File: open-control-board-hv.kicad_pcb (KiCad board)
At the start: 2 copper layers, 69 x 54 mm, 20 parts, among them J1 TE 160650-2, J2 TE 160650-2, J3 TE 160650-2, J4 TE 160650-2, J5 TE 160650-2, J6 TE 160650-2, K1 RT314A12, U2 ALDP112, U3 ALDP112, U4 ALDP112

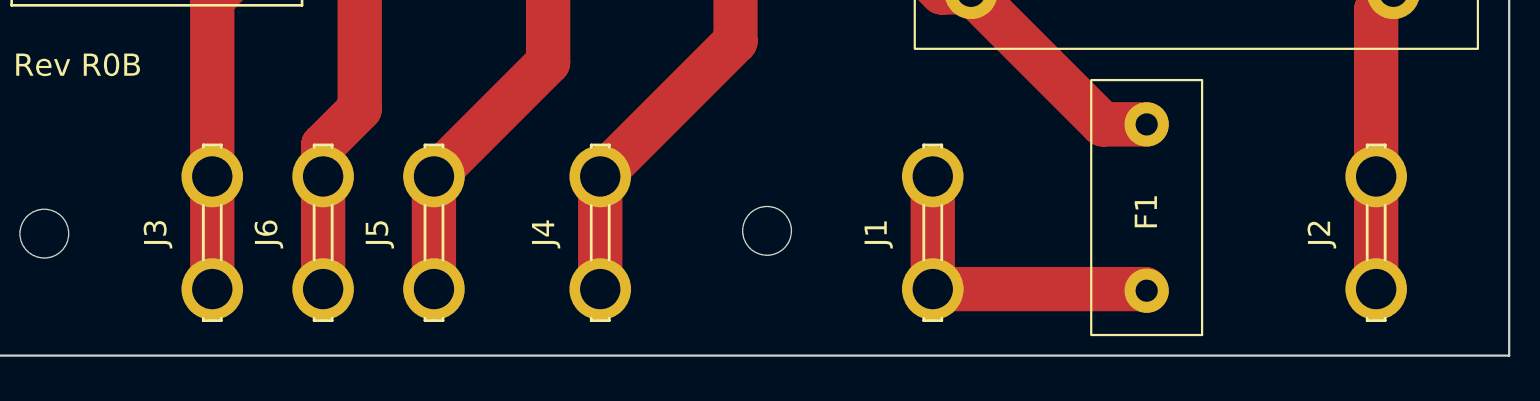
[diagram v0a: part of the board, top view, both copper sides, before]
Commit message: Updated with manufacturing data and switched footprint for fastons
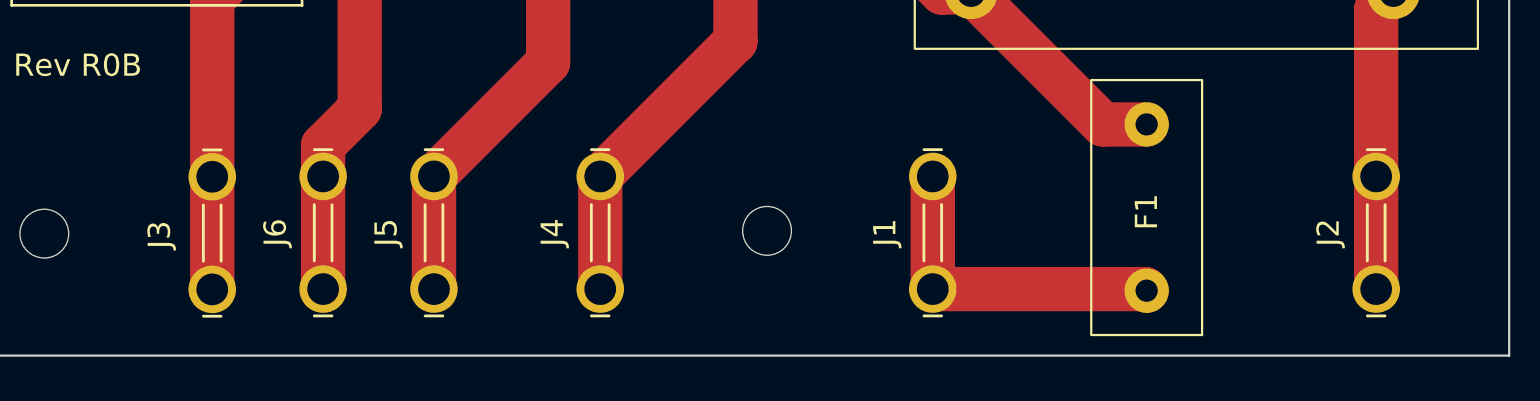
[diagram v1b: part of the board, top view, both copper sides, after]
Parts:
- J1, J2, J3, J4, J5, J6: footprint 1289:KEYSTONE_1289 -> 624091:TE_62409-1

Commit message: Cleanup
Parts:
- renumbered D4 to D2, D2 to D4, J6 to J4, J4 to J6, U4 to K2, U3 to K3, U2 to K4
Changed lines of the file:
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@@
     (property "ki_keywords" "connector")
     (attr through_hole)
-    (fp_text reference "J6" (at 0.0114 -2.151 90) (layer "F.SilkS")
+    (fp_text reference "J4" (at 0.0114 -2.151 90) (layer "F.SilkS")
         (effects (font (size 1.001661 1.001661) (thickness 0.15)))
     )
@@
       (stroke (width 0.127) (type solid)) (layer "F.Fab"))
     (pad "1" thru_hole circle (at -2.54 0 90) (size 2.145 2.145) (drill 1.43) (layers "*.Cu" "*.Mask")
-      (net 12 "Net-(J6-Pin_1)") (pinfunction "Pin_1") (pintype "passive") (solder_mask_margin 0.102))
+      (net 10 "Net-(J4-Pin_1)") (pinfunction "Pin_1") (pintype "passive") (solder_mask_margin 0.102))
     (pad "1" thru_hole circle (at 2.54 0 90) (size 2.145 2.145) (drill 1.43) (layers "*.Cu" "*.Mask")
-      (net 12 "Net-(J6-Pin_1)") (pinfunction "Pin_1") (pintype "passive") (solder_mask_margin 0.102))
+      (net 10 "Net-(J4-Pin_1)") (pinfunction "Pin_1") (pintype "passive") (solder_mask_margin 0.102))
   )
   (footprint "MountingHole:MountingHole_2.2mm_M2" (layer "F.Cu")
@@
     (property "ki_keywords" "diode")
     (attr through_hole exclude_from_pos_files)
-    (fp_text reference "D2" (at 4.3118 -0.0836) (layer "F.SilkS")
+    (fp_text reference "D4" (at 4.3118 -0.0836) (layer "F.SilkS")
         (effects (font (size 1 1) (thickness 0.15)))
     )
@@
     (property "Sheetfile" "open-control-board-hv.kicad_sch")
     (property "Sheetname" "")
-    (property "exclude_from_bom" "")
-    (property "ki_keywords" "ALDP112")
-    (attr through_hole exclude_from_pos_files exclude_from_bom)
-    (fp_text reference "U2" (at 2.3505 9.3091 unlocked) (layer "F.SilkS")
+    (property "ki_description" "Relay SPST, Normally Open, EN50005")
+    (property "ki_keywords" "Single Pole Relay SPST NO")
+    (attr through_hole exclude_from_pos_files)
+    (fp_text reference "K4" (at 2.3505 9.3091 unlocked) (layer "F.SilkS")
         (effects (font (size 1 1) (thickness 0.15)))
     )
@@
       (stroke (width 0.0254) (type solid)) (fill none) (layer "F.Fab"))
     (pad "1" thru_hole circle (at 4.7 0 180) (size 1.5494 1.5494) (drill 1.0414) (layers "*.Cu" "*.Mask")
-      (net 10 "Net-(J4-Pin_1)") (pinfunction "1") (pintype "unspecified"))
+      (net 12 "Net-(J6-Pin_1)") (pintype "passive"))
     (pad "2" thru_hole circle (at 4.7 7.0104 180) (size 1.5494 1.5494) (drill 1.0414) (layers "*.Cu" "*.Mask")
-      (net 6 "PH") (pinfunction "2") (pintype "unspecified"))
+      (net 6 "PH") (pintype "passive"))
     (pad "3" thru_hole circle (at 4.7 18.5166 180) (size 1.5494 1.5494) (drill 1.0414) (layers "*.Cu" "*.Mask")
-      (net 3 "FA7_CTRL") (pinfunction "3") (pintype "unspecified"))
+      (net 3 "FA7_CTRL") (pintype "passive"))
     (pad "4" thru_hole circle (at 0.001 18.5166 180) (size 1.5494 1.5494) (drill 1.0414) (layers "*.Cu" "*.Mask")
-      (net 1 "+12VA") (pinfunction "4") (pintype "unspecified"))
+      (net 1 "+12VA") (pintype "passive"))
   )
   (footprint "Relay_THT:Relay_SPDT_Schrack-RT1-16A-FormC_RM5mm" (layer "F.Cu")
@@
     (property "ki_keywords" "diode")
     (attr through_hole exclude_from_pos_files)
-    (fp_text reference "D4" (at 4.0832 -0.1598) (layer "F.SilkS")
+    (fp_text reference "D2" (at 4.0832 -0.1598) (layer "F.SilkS")
         (effects (font (size 1 1) (thickness 0.15)))
     )
@@
     (property "ki_keywords" "connector")
     (attr through_hole)
-    (fp_text reference "J4" (at 0.0114 -2.151 90) (layer "F.SilkS")
+    (fp_text reference "J6" (at 0.0114 -2.151 90) (layer "F.SilkS")
         (effects (font (size 1.001661 1.001661) (thickness 0.15)))
     )
@@
       (stroke (width 0.127) (type solid)) (layer "F.Fab"))
     (pad "1" thru_hole circle (at -2.54 0 90) (size 2.145 2.145) (drill 1.43) (layers "*.Cu" "*.Mask")
-      (net 10 "Net-(J4-Pin_1)") (pinfunction "Pin_1") (pintype "passive") (solder_mask_margin 0.102))
+      (net 12 "Net-(J6-Pin_1)") (pinfunction "Pin_1") (pintype "passive") (solder_mask_margin 0.102))
     (pad "1" thru_hole circle (at 2.54 0 90) (size 2.145 2.145) (drill 1.43) (layers "*.Cu" "*.Mask")
-      (net 10 "Net-(J4-Pin_1)") (pinfunction "Pin_1") (pintype "passive") (solder_mask_margin 0.102))
+      (net 12 "Net-(J6-Pin_1)") (pinfunction "Pin_1") (pintype "passive") (solder_mask_margin 0.102))
   )
   (footprint "ALDP112:PAN_ALD_PAN" (layer "F.Cu")
@@
     (property "Sheetfile" "open-control-board-hv.kicad_sch")
     (property "Sheetname" "")
-    (property "exclude_from_bom" "")
-    (property "ki_keywords" "ALDP112")
-    (attr through_hole exclude_from_pos_files exclude_from_bom)
-    (fp_text reference "U3" (at 2.3495 9.3091 unlocked) (layer "F.SilkS")
+    (property "ki_description" "Relay SPST, Normally Open, EN50005")
+    (property "ki_keywords" "Single Pole Relay SPST NO")
+    (attr through_hole exclude_from_pos_files)
+    (fp_text reference "K3" (at 2.3495 9.3091 unlocked) (layer "F.SilkS")
         (effects (font (size 1 1) (thickness 0.15)))
     )
@@
       (stroke (width 0.0254) (type solid)) (fill none) (layer "F.Fab"))
     (pad "1" thru_hole circle (at 4.7 0 180) (size 1.5494 1.5494) (drill 1.0414) (layers "*.Cu" "*.Mask")
-      (net 11 "Net-(J5-Pin_1)") (pinfunction "1") (pintype "unspecified"))
+      (net 11 "Net-(J5-Pin_1)") (pintype "passive"))
     (pad "2" thru_hole circle (at 4.7 7.0104 180) (size 1.5494 1.5494) (drill 1.0414) (layers "*.Cu" "*.Mask")
-      (net 6 "PH") (pinfunction "2") (pintype "unspecified"))
+      (net 6 "PH") (pintype "passive"))
     (pad "3" thru_hole circle (at 4.7 18.5166 180) (size 1.5494 1.5494) (drill 1.0414) (layers "*.Cu" "*.Mask")
-      (net 4 "FA8_CTRL") (pinfunction "3") (pintype "unspecified"))
+      (net 4 "FA8_CTRL") (pintype "passive"))
     (pad "4" thru_hole circle (at 0.001 18.5166 180) (size 1.5494 1.5494) (drill 1.0414) (layers "*.Cu" "*.Mask")
-      (net 1 "+12VA") (pinfunction "4") (pintype "unspecified"))
+      (net 1 "+12VA") (pintype "passive"))
   )
   (footprint "ECE05:ECE10" (layer "F.Cu")
@@
     (property "Sheetfile" "open-control-board-hv.kicad_sch")
     (property "Sheetname" "")
-    (property "exclude_from_bom" "")
-    (property "ki_keywords" "ALDP112")
-    (attr through_hole exclude_from_pos_files exclude_from_bom)
-    (fp_text reference "U4" (at 2.3495 9.3091 unlocked) (layer "F.SilkS")
+    (property "ki_description" "Relay SPST, Normally Open, EN50005")
+    (property "ki_keywords" "Single Pole Relay SPST NO")
+    (attr through_hole exclude_from_pos_files)
+    (fp_text reference "K2" (at 2.3495 9.3091 unlocked) (layer "F.SilkS")
         (effects (font (size 1 1) (thickness 0.15)))
     )
@@
       (stroke (width 0.0254) (type solid)) (fill none) (layer "F.Fab"))
     (pad "1" thru_hole circle (at 4.7 0 180) (size 1.5494 1.5494) (drill 1.0414) (layers "*.Cu" "*.Mask")
-      (net 12 "Net-(J6-Pin_1)") (pinfunction "1") (pintype "unspecified"))
+      (net 10 "Net-(J4-Pin_1)") (pintype "passive"))
     (pad "2" thru_hole circle (at 4.7 7.0104 180) (size 1.5494 1.5494) (drill 1.0414) (layers "*.Cu" "*.Mask")
-      (net 6 "PH") (pinfunction "2") (pintype "unspecified"))
+      (net 6 "PH") (pintype "passive"))
     (pad "3" thru_hole circle (at 4.7 18.5166 180) (size 1.5494 1.5494) (drill 1.0414) (layers "*.Cu" "*.Mask")
-      (net 5 "FA9_CTRL") (pinfunction "3") (pintype "unspecified"))
+      (net 5 "FA9_CTRL") (pintype "passive"))
     (pad "4" thru_hole circle (at 0.001 18.5166 180) (size 1.5494 1.5494) (drill 1.0414) (layers "*.Cu" "*.Mask")
-      (net 1 "+12VA") (pinfunction "4") (pintype "unspecified"))
+      (net 1 "+12VA") (pintype "passive"))
   )
   (footprint "1289:FRT 250T" (layer "F.Cu")
@@
   (segment (start 53.426 103.4764) (end 53.426 98.3964) (width 2) (layer "F.Cu") (net 9))
   (segment (start 47.176 89.1664) (end 54.676 89.1664) (width 2) (layer "F.Cu") (net 9))
-  (segment (start 77.025 87.793) (end 77.025 92.2974) (width 2) (layer "F.Cu") (net 10))
-  (segment (start 77.025 92.2974) (end 70.926 98.3964) (width 2) (layer "F.Cu") (net 10))
-  (segment (start 70.926 103.4764) (end 70.926 98.3964) (width 2) (layer "F.Cu") (net 10))
+  (segment (start 58.426 103.4764) (end 58.426 98.3964) (width 2) (layer "F.Cu") (net 10))
+  (segment (start 58.426 96.996329) (end 60.0755 95.346829) (width 2) (layer "F.Cu") (net 10))
+  (segment (start 58.426 98.3964) (end 58.426 96.996329) (width 2) (layer "F.Cu") (net 10))
+  (segment (start 60.0755 95.346829) (end 60.0755 87.7855) (width 2) (layer "F.Cu") (net 10))
   (segment (start 68.5755 93.2469) (end 63.426 98.3964) (width 2) (layer "F.Cu") (net 11))
   (segment (start 68.5755 87.7855) (end 68.5755 93.2469) (width 2) (layer "F.Cu") (net 11))
   (segment (start 63.426 103.4764) (end 63.426 98.3964) (width 2) (layer "F.Cu") (net 11))
-  (segment (start 58.426 103.4764) (end 58.426 98.3964) (width 2) (layer "F.Cu") (net 12))
-  (segment (start 58.426 96.996329) (end 60.0755 95.346829) (width 2) (layer "F.Cu") (net 12))
-  (segment (start 58.426 98.3964) (end 58.426 96.996329) (width 2) (layer "F.Cu") (net 12))
-  (segment (start 60.0755 95.346829) (end 60.0755 87.7855) (width 2) (layer "F.Cu") (net 12))
+  (segment (start 77.025 87.793) (end 77.025 92.2974) (width 2) (layer "F.Cu") (net 12))
+  (segment (start 77.025 92.2974) (end 70.926 98.3964) (width 2) (layer "F.Cu") (net 12))
+  (segment (start 70.926 103.4764) (end 70.926 98.3964) (width 2) (layer "F.Cu") (net 12))
   (segment (start 84.1 63.025) (end 79.0564 63.025) (width 0.4) (layer "F.Cu") (net 13))
   (segment (start 71.0078 54.9764) (end 57.926 54.9764) (width 0.4) (layer "F.Cu") (net 13))

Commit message: R0C
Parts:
- moved U1 1.02 mm to (111.5, 54.3)
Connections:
- F1 pad 1: PH_PRE_FUSE -> PH
- F1 pad 2: PH -> PH_FUSED
- J1 pad 1: PH_PRE_FUSE -> PH
- K1 pad 12: unconnected-(K1-Pad12) -> PH
- U1 pad 2: PH -> PH_FUSED
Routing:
- net PH: track 56.1 -> 119.6 mm
- net Net-(J3-Pin_1): track 22.3 -> 0.00 mm
- net Net-(J6-Pin_1): track 18.2 -> 36.4 mm
- net Net-(J5-Pin_1): track 17.8 -> 35.6 mm
- net Net-(J4-Pin_1): track 16.4 -> 32.7 mm
- net N: track 13.7 -> 28.8 mm
- net PH_PRE_FUSE: track 14.8 -> 0.00 mm
- net PH_FUSED: track 0.00 -> 9.52 mm
- net GND1: track 36.9 -> 38.4 mm
- net +12VA: track 91.0 -> 92.1 mm
- added copper zone on B.Cu, net Net-(J3-Pin_1)
- added copper zone on F.Cu, net Net-(J3-Pin_1)
- added copper zone on B.Cu, net PH
- added copper zone on F.Cu, net PH
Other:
- board text added: "Rev R0D"
- board text removed: "Rev R0B"
